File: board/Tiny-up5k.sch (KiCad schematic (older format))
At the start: 37 parts, among them J1 CONN_01X14, J2 CONN_01X14, J5 Prog, SW1 SW_Push, U1 ICE40UP5K-SG48ITR, U2 MIC5504-3.3YM5, U3 DSC6001CI2A-016.0000T, U4 MIC5504-1.2YM5, U5 AT25xxx-MA, U6 USB_OTG

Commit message: change j5 footprint for default kicad footprint
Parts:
- J5: footprint Pin_Headers:Pin_Header_Straight_2x03_Pitch2.54mm_SMD -> Connector_PinHeader_2.54mm:PinHeader_2x03_P2.54mm_Vertical_SMD
- U5: manf# SST25VF016B-50-4C-QAF-T -> SST25VF016B-50-4C-QAF-T
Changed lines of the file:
@@
 F 0 "J5" H 11200 1050 50  0000 C CNN
 F 1 "Prog" H 11200 650 50  0000 C CNN
-F 2 "Pin_Headers:Pin_Header_Straight_2x03_Pitch2.54mm_SMD" H 11150 850 50  0001 C CNN
+F 2 "Connector_PinHeader_2.54mm:PinHeader_2x03_P2.54mm_Vertical_SMD" H 11150 850 50  0001 C CNN
 F 3 "" H 11150 850 50  0001 C CNN
 	1    11150 850
@@
 F 2 "Package_DFN_QFN:DFN-8-1EP_3x2mm_P0.5mm_EP1.75x1.45mm" H 7350 4100 50  0001 C CNN
 F 3 "http://ww1.microchip.com/downloads/en/DeviceDoc/Atmel-8707-SEEPROM-AT25010B-020B-040B-Datasheet.pdf" H 7350 4100 50  0001 C CNN
-F 4 " SST25VF016B-50-4C-QAF-T" H 7350 4100 50  0001 C CNN "manf#"
+F 4 "SST25VF016B-50-4C-QAF-T" H 7350 4100 50  0001 C CNN "manf#"
 	1    7350 4100
 	1    0    0    -1

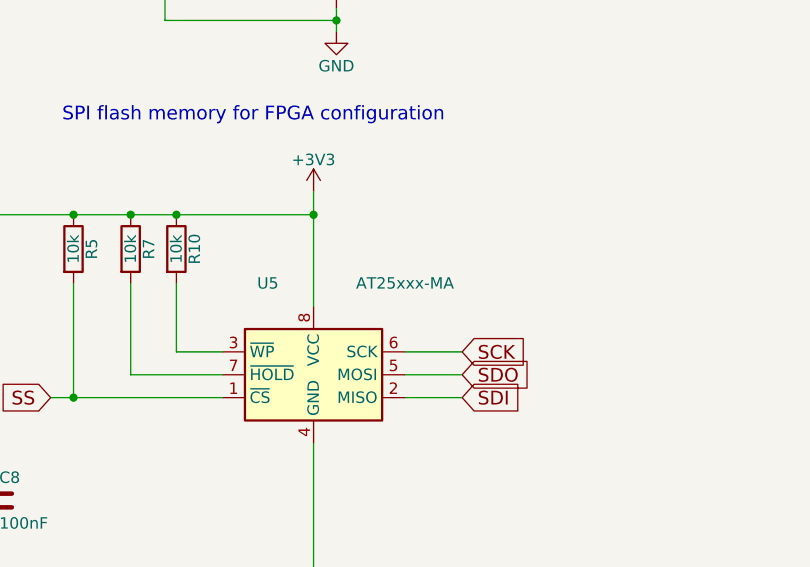
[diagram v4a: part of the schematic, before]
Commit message: Improve the frabrication layout. Make some trace wider
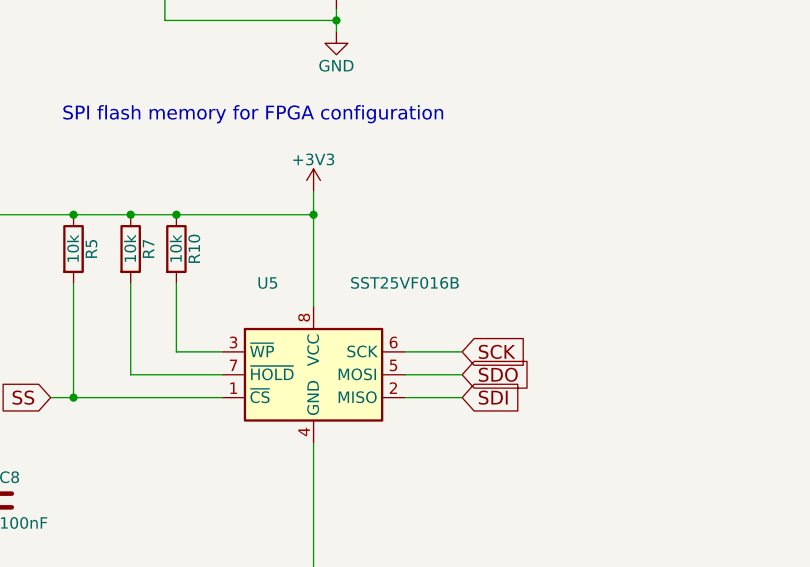
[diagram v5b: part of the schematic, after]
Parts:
- U5: value AT25xxx-MA -> SST25VF016B
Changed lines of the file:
@@
 P 7350 4100
 F 0 "U5" H 7150 4500 50  0000 C CNN
-F 1 "AT25xxx-MA" H 7750 4500 50  0000 C CNN
+F 1 "SST25VF016B" H 7750 4500 50  0000 C CNN
 F 2 "Package_DFN_QFN:DFN-8-1EP_3x2mm_P0.5mm_EP1.75x1.45mm" H 7350 4100 50  0001 C CNN
 F 3 "http://ww1.microchip.com/downloads/en/DeviceDoc/Atmel-8707-SEEPROM-AT25010B-020B-040B-Datasheet.pdf" H 7350 4100 50  0001 C CNN

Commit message: Replaced footprint of spi flash chip
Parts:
- U5: footprint Package_DFN_QFN:DFN-8-1EP_3x2mm_P0.5mm_EP1.75x1.45mm -> Package_SON:WSON-8-1EP_6x5mm_P1.27mm_EP3.4x4mm
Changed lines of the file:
@@
 F 0 "U5" H 7150 4500 50  0000 C CNN
 F 1 "SST25VF016B" H 7750 4500 50  0000 C CNN
-F 2 "Package_DFN_QFN:DFN-8-1EP_3x2mm_P0.5mm_EP1.75x1.45mm" H 7350 4100 50  0001 C CNN
+F 2 "Package_SON:WSON-8-1EP_6x5mm_P1.27mm_EP3.4x4mm" H 7350 4100 39  0001 C CNN
 F 3 "http://ww1.microchip.com/downloads/en/DeviceDoc/Atmel-8707-SEEPROM-AT25010B-020B-040B-Datasheet.pdf" H 7350 4100 50  0001 C CNN
 F 4 "SST25VF016B-50-4C-QAF-T" H 7350 4100 50  0001 C CNN "manf#"

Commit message: Also fix SMD pad that should get no solder
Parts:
- J5: footprint Connector_PinHeader_2.54mm:PinHeader_2x03_P2.54mm_Vertical_SMD -> board:PinHeader_2x03_P2.54mm_Vertical_SMD_NoSolder
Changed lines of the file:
@@
 F 0 "J5" H 11200 1050 50  0000 C CNN
 F 1 "Prog" H 11200 650 50  0000 C CNN
-F 2 "Connector_PinHeader_2.54mm:PinHeader_2x03_P2.54mm_Vertical_SMD" H 11150 850 50  0001 C CNN
+F 2 "board:PinHeader_2x03_P2.54mm_Vertical_SMD_NoSolder" H 11150 850 50  0001 C CNN
 F 3 "" H 11150 850 50  0001 C CNN
 	1    11150 850

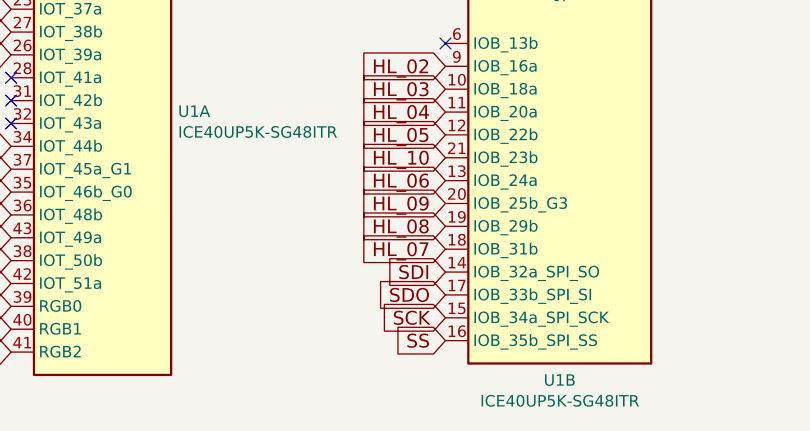
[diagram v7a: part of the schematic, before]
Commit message: Fix SPI line and send rev03 to aisler
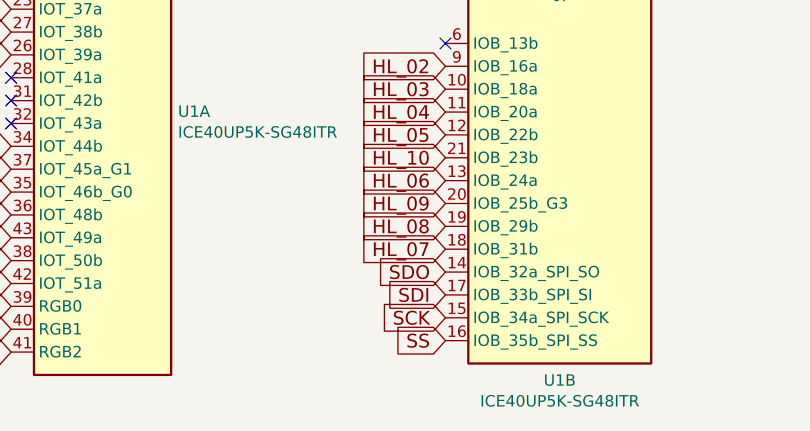
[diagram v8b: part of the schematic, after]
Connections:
- net SDI: now also U1.17 (IOB_33b_SPI_SI); no longer U1.14 (IOB_32a_SPI_SO)
- net SDO: now also U1.14 (IOB_32a_SPI_SO); no longer U1.17 (IOB_33b_SPI_SI)
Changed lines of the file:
@@
 $EndComp
 Text GLabel 11800 7900 0    60   Input ~ 0
-SDO
+SDI
 Text GLabel 11800 8000 0    60   Input ~ 0
 SCK
@@
 CRESET_B
 Text GLabel 11800 7800 0    60   Input ~ 0
-SDI
+SDO
 Text GLabel 13950 5400 0    60   Input ~ 0
 USB_P
